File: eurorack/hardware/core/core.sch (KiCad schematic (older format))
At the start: 48 parts, among them J1 ConnNW, J2 ConnSW, J3 ConnNE, J4 ConnSE, J5 Power, J6 SWD, SW1 Reset, SW2 Boot0, U1 STM32F427VGT6, U2 TLV320AIC23BPW, U3 LM1117F-3.3, U4 LM4040C10IDBZR, Y1 Crystal

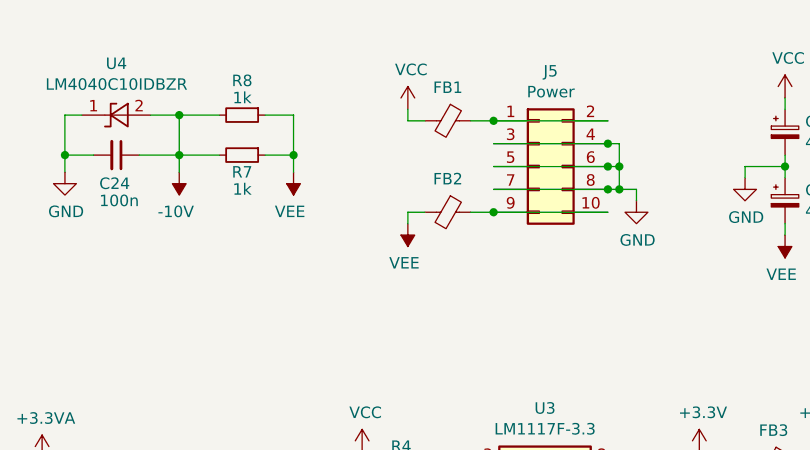
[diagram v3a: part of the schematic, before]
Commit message: Add protective diodes
Signed-off-by: Petr Horacek <hrck@protonmail.com>
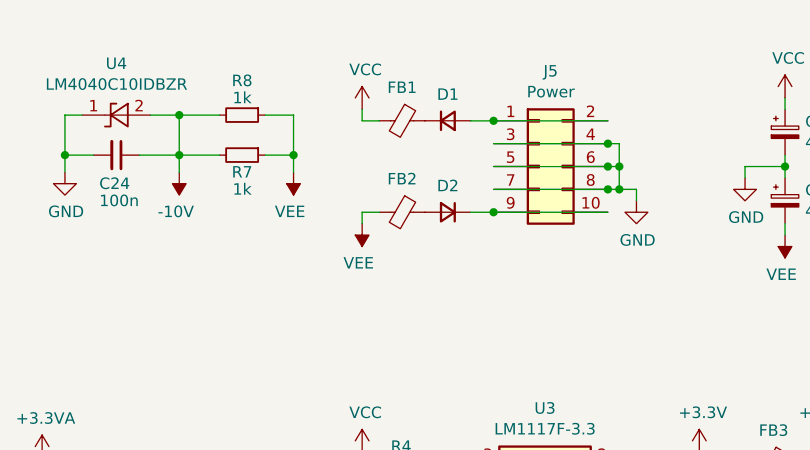
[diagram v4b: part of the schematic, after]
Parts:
- added D1, D2: D_Small, Diode_SMD:D_SOD-123, symbol Device:D_Small
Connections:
- net at J5.1 (Pin_1), J5.2 (Pin_2): now also D1.2 (A); no longer FB1.1
- net at J5.10 (Pin_10), J5.9 (Pin_9): now also D2.1 (K); no longer FB2.1
- new net: D1.1 (K), FB1.1
- new net: D2.2 (A), FB2.1
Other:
- moved on the sheet: FB1, FB2
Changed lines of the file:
@@
 L Device:Ferrite_Bead_Small FB1
 U 1 1 60CA6A97
-P 9150 1075
-F 0 "FB1" V 9005 1075 50  0000 C CNN
-F 1 "Ferrite_Bead_Small" V 9004 1075 50  0001 C CNN
-F 2 "Inductor_SMD:L_0805_2012Metric" V 9080 1075 50  0001 C CNN
-F 3 "~" H 9150 1075 50  0001 C CNN
-	1    9150 1075
+P 8950 1075
+F 0 "FB1" V 8805 1075 50  0000 C CNN
+F 1 "Ferrite_Bead_Small" V 8804 1075 50  0001 C CNN
+F 2 "Inductor_SMD:L_0805_2012Metric" V 8880 1075 50  0001 C CNN
+F 3 "~" H 8950 1075 50  0001 C CNN
+	1    8950 1075
 	0    1    1    0
 $EndComp
@@
 L Device:Ferrite_Bead_Small FB2
 U 1 1 60CA755F
-P 9150 1475
-F 0 "FB2" V 9005 1475 50  0000 C CNN
-F 1 "Ferrite_Bead_Small" V 9004 1475 50  0001 C CNN
-F 2 "Inductor_SMD:L_0805_2012Metric" V 9080 1475 50  0001 C CNN
-F 3 "~" H 9150 1475 50  0001 C CNN
-	1    9150 1475
+P 8950 1475
+F 0 "FB2" V 8805 1475 50  0000 C CNN
+F 1 "Ferrite_Bead_Small" V 8804 1475 50  0001 C CNN
+F 2 "Inductor_SMD:L_0805_2012Metric" V 8880 1475 50  0001 C CNN
+F 3 "~" H 8950 1475 50  0001 C CNN
+	1    8950 1475
 	0    1    1    0
 $EndComp
@@
 L power:VEE #PWR0106
 U 1 1 60CB1BF4
-P 8975 1525
-F 0 "#PWR0106" H 8975 1375 50  0001 C CNN
-F 1 "VEE" H 8990 1698 50  0000 C CNN
-F 2 "" H 8975 1525 50  0001 C CNN
-F 3 "" H 8975 1525 50  0001 C CNN
-	1    8975 1525
+P 8775 1525
+F 0 "#PWR0106" H 8775 1375 50  0001 C CNN
+F 1 "VEE" H 8790 1698 50  0000 C CNN
+F 2 "" H 8775 1525 50  0001 C CNN
+F 3 "" H 8775 1525 50  0001 C CNN
+	1    8775 1525
 	-1   0    0    1
 $EndComp
@@
 L power:VCC #PWR0107
 U 1 1 60CB285D
-P 8975 1025
-F 0 "#PWR0107" H 8975 875 50  0001 C CNN
-F 1 "VCC" H 8990 1198 50  0000 C CNN
-F 2 "" H 8975 1025 50  0001 C CNN
-F 3 "" H 8975 1025 50  0001 C CNN
-	1    8975 1025
-	1    0    0    -1
-$EndComp
-Wire Wire Line
-	8975 1025 8975 1075
-Wire Wire Line
-	8975 1075 9050 1075
-Wire Wire Line
-	9050 1475 8975 1475
-Wire Wire Line
-	8975 1475 8975 1525
+P 8775 1025
+F 0 "#PWR0107" H 8775 875 50  0001 C CNN
+F 1 "VCC" H 8790 1198 50  0000 C CNN
+F 2 "" H 8775 1025 50  0001 C CNN
+F 3 "" H 8775 1025 50  0001 C CNN
+	1    8775 1025
+	1    0    0    -1
+$EndComp
+Wire Wire Line
+	8775 1025 8775 1075
+Wire Wire Line
+	8775 1075 8850 1075
+Wire Wire Line
+	8850 1475 8775 1475
+Wire Wire Line
+	8775 1475 8775 1525
 $Comp
 L power:GND #PWR0108
@@
 Text GLabel 4450 2250 2    50   Input ~ 0
 PIN5
+$Comp
+L Device:D_Small D1
+U 1 1 61D1306A
+P 9150 1075
+F 0 "D1" H 9150 1190 50  0000 C CNN
+F 1 "D_Small" H 9150 1191 50  0001 C CNN
+F 2 "Diode_SMD:D_SOD-123" V 9150 1075 50  0001 C CNN
+F 3 "~" V 9150 1075 50  0001 C CNN
+	1    9150 1075
+	1    0    0    -1
+$EndComp
+$Comp
+L Device:D_Small D2
+U 1 1 61D4FE28
+P 9150 1475
+F 0 "D2" H 9150 1360 50  0000 C CNN
+F 1 "D_Small" H 9150 1591 50  0001 C CNN
+F 2 "Diode_SMD:D_SOD-123" V 9150 1475 50  0001 C CNN
+F 3 "~" V 9150 1475 50  0001 C CNN
+	1    9150 1475
+	-1   0    0    1
+$EndComp
 $EndSCHEMATC

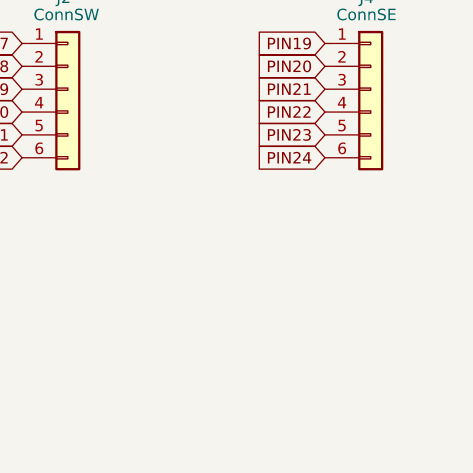
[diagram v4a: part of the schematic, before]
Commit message: Add mounting holes
Signed-off-by: Petr Horacek <hrck@protonmail.com>
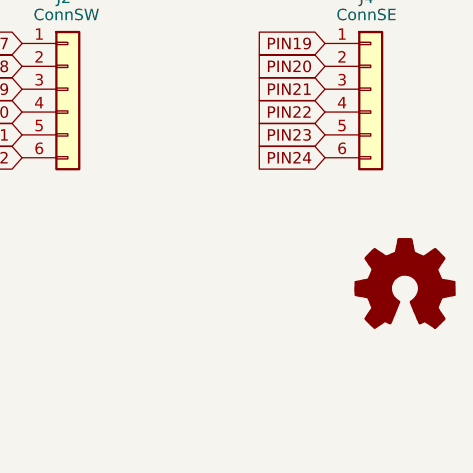
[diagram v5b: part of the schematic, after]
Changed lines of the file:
@@
 Sheet 1 1
 Title ""
-Date ""
-Rev ""
-Comp ""
-Comment1 ""
-Comment2 ""
-Comment3 ""
+Date "2021-05-01"
+Rev "1"
+Comp "Petr Horáček"
+Comment1 "hrck@protonmail.com"
+Comment2 "github.com/zlosynth/TODO"
+Comment3 "cc-by-sa"
 Comment4 ""
 $EndDescr
@@
 	-1   0    0    1
 $EndComp
+$Comp
+L Graphic:Logo_Open_Hardware_Small #LOGO1
+U 1 1 61E1BF99
+P 10900 6875
+F 0 "#LOGO1" H 10900 7150 50  0001 C CNN
+F 1 "Logo_Open_Hardware_Small" H 10900 6650 50  0001 C CNN
+F 2 "Symbol:OSHW-Symbol_6.7x6mm_Copper" H 10900 7169 50  0001 C CNN
+F 3 "~" H 10900 6875 50  0001 C CNN
+	1    10900 6875
+	1    0    0    -1
+$EndComp
 $EndSCHEMATC

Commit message: Add no connect flags to the schema
Signed-off-by: Petr Horacek <hrck@protonmail.com>
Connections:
- no-connect marks 7 -> 53
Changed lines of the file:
@@
 	-1   0    0    1
 $EndComp
-$Comp
-L Graphic:Logo_Open_Hardware_Small #LOGO1
-U 1 1 61E1BF99
-P 10900 6875
-F 0 "#LOGO1" H 10900 7150 50  0001 C CNN
-F 1 "Logo_Open_Hardware_Small" H 10900 6650 50  0001 C CNN
-F 2 "Symbol:OSHW-Symbol_6.7x6mm_Copper" H 10900 7169 50  0001 C CNN
-F 3 "~" H 10900 6875 50  0001 C CNN
-	1    10900 6875
-	1    0    0    -1
-$EndComp
+NoConn ~ 4450 2150
+NoConn ~ 4450 2450
+NoConn ~ 4450 3150
+NoConn ~ 4450 3350
+NoConn ~ 4450 3450
+NoConn ~ 4450 3550
+NoConn ~ 4450 3650
+NoConn ~ 4450 3750
+NoConn ~ 4450 3850
+NoConn ~ 4450 3950
+NoConn ~ 4450 4050
+NoConn ~ 2650 3150
+NoConn ~ 2650 3250
+NoConn ~ 2650 3350
+NoConn ~ 2650 3450
+NoConn ~ 2650 3550
+NoConn ~ 2650 3650
+NoConn ~ 2650 3750
+NoConn ~ 2650 3850
+NoConn ~ 2650 3950
+NoConn ~ 2650 4050
+NoConn ~ 2650 4150
+NoConn ~ 2650 4250
+NoConn ~ 2650 4350
+NoConn ~ 2650 4450
+NoConn ~ 2650 4650
+NoConn ~ 2650 4750
+NoConn ~ 2650 4850
+NoConn ~ 2650 4950
+NoConn ~ 2650 5250
+NoConn ~ 2650 5350
+NoConn ~ 2650 5450
+NoConn ~ 2650 5550
+NoConn ~ 2650 5650
+NoConn ~ 2650 5750
+NoConn ~ 2650 5850
+NoConn ~ 2650 5950
+NoConn ~ 2650 6050
+NoConn ~ 2650 6150
+NoConn ~ 4450 5350
+NoConn ~ 4450 5450
+NoConn ~ 4450 5850
+NoConn ~ 4450 5950
+NoConn ~ 4450 6050
+NoConn ~ 4450 6150
+NoConn ~ 7875 4250
 $EndSCHEMATC

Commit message: Add bill of materials
Signed-off-by: Petr Horacek <hrck@protonmail.com>
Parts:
- C1, C2: LCSC Part # (none) -> C1554
- C10, C20: LCSC Part # (none) -> C52923
- C11, C12, C13, C14, C15, C16, C17, C18, C19, C21, C22, C23: LCSC Part # (none) -> C1525
- C24: LCSC Part # (none) -> C49678
- C3, C4, C7: LCSC Part # (none) -> C23630
- C5, C6, C8, C9: LCSC Part # (none) -> C129570
- D1, D2: LCSC Part # (none) -> C8598
- FB1, FB2, FB3: LCSC Part # (none) -> C1017
- R1: LCSC Part # (none) -> C25118
- R2, R3: LCSC Part # (none) -> C25744
- R4: LCSC Part # (none) -> C22810
- R5, R6: LCSC Part # (none) -> C25879
- R7, R8: LCSC Part # (none) -> C17513
- SW1, SW2: LCSC Part # (none) -> C115357
- U4: LCSC Part # (none) -> C201738
- Y1: LCSC Part # (none) -> C115962
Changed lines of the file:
@@
 F 2 "Capacitor_SMD:C_0603_1608Metric" H 2200 1900 50  0001 C CNN
 F 3 "~" H 2200 1900 50  0001 C CNN
+F 4 "C23630" H 2200 1900 50  0001 C CNN "LCSC Part #"
 	1    2200 1900
 	1    0    0    -1
@@
 F 2 "Capacitor_Tantalum_SMD:CP_EIA-3216-18_Kemet-A" H 9125 2750 50  0001 C CNN
 F 3 "~" H 9125 2750 50  0001 C CNN
+F 4 "C129570" H 9125 2750 50  0001 C CNN "LCSC Part #"
 	1    9125 2750
 	1    0    0    -1
@@
 F 2 "Capacitor_Tantalum_SMD:CP_EIA-3216-18_Kemet-A" H 9925 2725 50  0001 C CNN
 F 3 "~" H 9925 2725 50  0001 C CNN
+F 4 "C129570" H 9925 2725 50  0001 C CNN "LCSC Part #"
 	1    9925 2725
 	1    0    0    -1
@@
 F 2 "Capacitor_Tantalum_SMD:CP_EIA-3216-18_Kemet-A" H 10625 1425 50  0001 C CNN
 F 3 "~" H 10625 1425 50  0001 C CNN
+F 4 "C129570" H 10625 1425 50  0001 C CNN "LCSC Part #"
 	1    10625 1425
 	1    0    0    -1
@@
 F 2 "Capacitor_Tantalum_SMD:CP_EIA-3216-18_Kemet-A" H 10625 1125 50  0001 C CNN
 F 3 "~" H 10625 1125 50  0001 C CNN
+F 4 "C129570" H 10625 1125 50  0001 C CNN "LCSC Part #"
 	1    10625 1125
 	1    0    0    -1
@@
 F 2 "Inductor_SMD:L_0805_2012Metric" V 8880 1075 50  0001 C CNN
 F 3 "~" H 8950 1075 50  0001 C CNN
+F 4 "C1017" H 8950 1075 50  0001 C CNN "LCSC Part #"
 	1    8950 1075
 	0    1    1    0
@@
 F 2 "Inductor_SMD:L_0805_2012Metric" V 8880 1475 50  0001 C CNN
 F 3 "~" H 8950 1475 50  0001 C CNN
+F 4 "C1017" H 8950 1475 50  0001 C CNN "LCSC Part #"
 	1    8950 1475
 	0    1    1    0
@@
 F 2 "Capacitor_SMD:C_0603_1608Metric" H 10250 2725 50  0001 C CNN
 F 3 "~" H 10250 2725 50  0001 C CNN
+F 4 "C23630" H 10250 2725 50  0001 C CNN "LCSC Part #"
 	1    10250 2725
 	1    0    0    -1
@@
 F 2 "Resistor_SMD:R_0603_1608Metric" H 8950 2575 50  0001 C CNN
 F 3 "~" H 8950 2575 50  0001 C CNN
+F 4 "C22810" H 8950 2575 50  0001 C CNN "LCSC Part #"
 	1    8950 2575
 	0    1    1    0
@@
 F 2 "Inductor_SMD:L_0805_2012Metric" V 10505 2575 50  0001 C CNN
 F 3 "~" H 10575 2575 50  0001 C CNN
+F 4 "C1017" H 10575 2575 50  0001 C CNN "LCSC Part #"
 	1    10575 2575
 	0    1    1    0
@@
 F 2 "Capacitor_SMD:C_0402_1005Metric" H 2875 7175 50  0001 C CNN
 F 3 "~" H 2875 7175 50  0001 C CNN
+F 4 "C52923" H 2875 7175 50  0001 C CNN "LCSC Part #"
 	1    2875 7175
 	1    0    0    -1
@@
 F 2 "Capacitor_SMD:C_0402_1005Metric" H 3250 7175 50  0001 C CNN
 F 3 "~" H 3250 7175 50  0001 C CNN
+F 4 "C1525" H 3250 7175 50  0001 C CNN "LCSC Part #"
 	1    3250 7175
 	1    0    0    -1
@@
 F 2 "Capacitor_SMD:C_0402_1005Metric" H 3650 7175 50  0001 C CNN
 F 3 "~" H 3650 7175 50  0001 C CNN
+F 4 "C1525" H 3650 7175 50  0001 C CNN "LCSC Part #"
 	1    3650 7175
 	1    0    0    -1
@@
 F 2 "Capacitor_SMD:C_0402_1005Metric" H 4050 7175 50  0001 C CNN
 F 3 "~" H 4050 7175 50  0001 C CNN
+F 4 "C1525" H 4050 7175 50  0001 C CNN "LCSC Part #"
 	1    4050 7175
 	1    0    0    -1
@@
 F 2 "Capacitor_SMD:C_0402_1005Metric" H 4450 7175 50  0001 C CNN
 F 3 "~" H 4450 7175 50  0001 C CNN
+F 4 "C1525" H 4450 7175 50  0001 C CNN "LCSC Part #"
 	1    4450 7175
 	1    0    0    -1
@@
 F 2 "Capacitor_SMD:C_0402_1005Metric" H 4850 7175 50  0001 C CNN
 F 3 "~" H 4850 7175 50  0001 C CNN
+F 4 "C1525" H 4850 7175 50  0001 C CNN "LCSC Part #"
 	1    4850 7175
 	1    0    0    -1
@@
 F 2 "Capacitor_SMD:C_0402_1005Metric" H 5250 7175 50  0001 C CNN
 F 3 "~" H 5250 7175 50  0001 C CNN
+F 4 "C1525" H 5250 7175 50  0001 C CNN "LCSC Part #"
 	1    5250 7175
 	1    0    0    -1
@@
 F 2 "Capacitor_SMD:C_0402_1005Metric" H 5650 7175 50  0001 C CNN
 F 3 "~" H 5650 7175 50  0001 C CNN
+F 4 "C1525" H 5650 7175 50  0001 C CNN "LCSC Part #"
 	1    5650 7175
 	1    0    0    -1
@@
 F 2 "Capacitor_SMD:C_0402_1005Metric" H 6050 7175 50  0001 C CNN
 F 3 "~" H 6050 7175 50  0001 C CNN
+F 4 "C1525" H 6050 7175 50  0001 C CNN "LCSC Part #"
 	1    6050 7175
 	1    0    0    -1
@@
 F 2 "Capacitor_SMD:C_0402_1005Metric" H 6450 7175 50  0001 C CNN
 F 3 "~" H 6450 7175 50  0001 C CNN
+F 4 "C1525" H 6450 7175 50  0001 C CNN "LCSC Part #"
 	1    6450 7175
 	1    0    0    -1
@@
 F 2 "Resistor_SMD:R_0402_1005Metric" H 6175 2800 50  0001 C CNN
 F 3 "~" H 6175 2800 50  0001 C CNN
+F 4 "C25879" H 6175 2800 50  0001 C CNN "LCSC Part #"
 	1    6175 2800
 	1    0    0    -1
@@
 F 2 "Resistor_SMD:R_0402_1005Metric" H 5925 2800 50  0001 C CNN
 F 3 "~" H 5925 2800 50  0001 C CNN
+F 4 "C25879" H 5925 2800 50  0001 C CNN "LCSC Part #"
 	1    5925 2800
 	1    0    0    -1
@@
 F 2 "Capacitor_SMD:C_0603_1608Metric" H 1875 1900 50  0001 C CNN
 F 3 "~" H 1875 1900 50  0001 C CNN
+F 4 "C23630" H 1875 1900 50  0001 C CNN "LCSC Part #"
 	1    1875 1900
 	1    0    0    -1
@@
 F 2 "Resistor_SMD:R_0402_1005Metric" H 1225 7150 50  0001 C CNN
 F 3 "~" H 1225 7150 50  0001 C CNN
+F 4 "C25744" H 1225 7150 50  0001 C CNN "LCSC Part #"
 	1    1225 7150
 	0    1    1    0
@@
 F 2 "Button_Switch_SMD:SW_Push_SPST_NO_Alps_SKRK" H 1625 7350 50  0001 C CNN
 F 3 "~" H 1625 7350 50  0001 C CNN
+F 4 "C115357" H 1625 7150 50  0001 C CNN "LCSC Part #"
 	1    1625 7150
 	1    0    0    -1
@@
 F 2 "Resistor_SMD:R_0402_1005Metric" H 1725 6150 50  0001 C CNN
 F 3 "~" H 1725 6150 50  0001 C CNN
+F 4 "C25744" H 1725 6150 50  0001 C CNN "LCSC Part #"
 	1    1725 6150
 	0    1    1    0
@@
 F 2 "Button_Switch_SMD:SW_Push_SPST_NO_Alps_SKRK" H 1325 6350 50  0001 C CNN
 F 3 "~" H 1325 6350 50  0001 C CNN
+F 4 "C115357" H 1325 6150 50  0001 C CNN "LCSC Part #"
 	1    1325 6150
 	1    0    0    -1
@@
 F 2 "Crystal:Crystal_SMD_5032-2Pin_5.0x3.2mm" H 1375 3250 50  0001 C CNN
 F 3 "~" H 1375 3250 50  0001 C CNN
+F 4 "C115962" H 1375 3250 50  0001 C CNN "LCSC Part #"
 	1    1375 3250
 	1    0    0    -1
@@
 F 2 "Capacitor_SMD:C_0402_1005Metric" H 1175 3450 50  0001 C CNN
 F 3 "~" H 1175 3450 50  0001 C CNN
+F 4 "C1554" H 1175 3450 50  0001 C CNN "LCSC Part #"
 	1    1175 3450
 	1    0    0    -1
@@
 F 2 "Capacitor_SMD:C_0402_1005Metric" H 1575 3450 50  0001 C CNN
 F 3 "~" H 1575 3450 50  0001 C CNN
+F 4 "C1554" H 1575 3450 50  0001 C CNN "LCSC Part #"
 	1    1575 3450
 	1    0    0    -1
@@
 F 2 "Resistor_SMD:R_0402_1005Metric" H 1175 3000 50  0001 C CNN
 F 3 "~" H 1175 3000 50  0001 C CNN
+F 4 "C25118" H 1175 3000 50  0001 C CNN "LCSC Part #"
 	1    1175 3000
 	1    0    0    -1
@@
 F 2 "Capacitor_SMD:C_0402_1005Metric" H 6050 6425 50  0001 C CNN
 F 3 "~" H 6050 6425 50  0001 C CNN
+F 4 "C1525" H 6050 6425 50  0001 C CNN "LCSC Part #"
 	1    6050 6425
 	1    0    0    -1
@@
 F 2 "Capacitor_SMD:C_0402_1005Metric" H 5650 6425 50  0001 C CNN
 F 3 "~" H 5650 6425 50  0001 C CNN
+F 4 "C1525" H 5650 6425 50  0001 C CNN "LCSC Part #"
 	1    5650 6425
 	1    0    0    -1
@@
 F 2 "Capacitor_SMD:C_0402_1005Metric" H 5250 6425 50  0001 C CNN
 F 3 "~" H 5250 6425 50  0001 C CNN
+F 4 "C1525" H 5250 6425 50  0001 C CNN "LCSC Part #"
 	1    5250 6425
 	1    0    0    -1
@@
 F 2 "Capacitor_SMD:C_0402_1005Metric" H 4875 6425 50  0001 C CNN
 F 3 "~" H 4875 6425 50  0001 C CNN
+F 4 "C52923" H 4875 6425 50  0001 C CNN "LCSC Part #"
 	1    4875 6425
 	1    0    0    -1
@@
 F 2 "Package_TO_SOT_SMD:SOT-23" H 7700 850 50  0001 C CIN
 F 3 "http://www.ti.com/lit/ds/symlink/lm4040-n.pdf" H 7700 1050 50  0001 C CIN
+F 4 "C201738" H 7700 1050 50  0001 C CNN "LCSC Part #"
 	1    7700 1050
 	-1   0    0    1
@@
 F 2 "Capacitor_SMD:C_0805_2012Metric" H 7700 1225 50  0001 C CNN
 F 3 "~" H 7700 1225 50  0001 C CNN
+F 4 "C49678" H 7700 1225 50  0001 C CNN "LCSC Part #"
 	1    7700 1225
 	0    1    1    0
@@
 F 2 "Resistor_SMD:R_0805_2012Metric" H 8250 1050 50  0001 C CNN
 F 3 "~" H 8250 1050 50  0001 C CNN
+F 4 "C17513" H 8250 1050 50  0001 C CNN "LCSC Part #"
 	1    8250 1050
 	0    1    1    0
@@
 F 2 "Resistor_SMD:R_0805_2012Metric" H 8250 1225 50  0001 C CNN
 F 3 "~" H 8250 1225 50  0001 C CNN
+F 4 "C17513" H 8250 1225 50  0001 C CNN "LCSC Part #"
 	1    8250 1225
 	0    1    1    0
@@
 F 2 "Diode_SMD:D_SOD-123" V 9150 1075 50  0001 C CNN
 F 3 "~" V 9150 1075 50  0001 C CNN
+F 4 "C8598" H 9150 1075 50  0001 C CNN "LCSC Part #"
 	1    9150 1075
 	1    0    0    -1
@@
 F 2 "Diode_SMD:D_SOD-123" V 9150 1475 50  0001 C CNN
 F 3 "~" V 9150 1475 50  0001 C CNN
+F 4 "C8598" H 9150 1475 50  0001 C CNN "LCSC Part #"
 	1    9150 1475
 	-1   0    0    1
